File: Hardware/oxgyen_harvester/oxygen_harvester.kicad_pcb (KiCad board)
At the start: 2 copper layers, 154.9 x 111.8 mm, 79 parts, among them J1 Barrel_Jack_Switch, J10 Screw_Terminal_01x02, J11 Screw_Terminal_01x02, J12 Screw_Terminal_01x02, J13 Screw_Terminal_01x02, J14 Screw_Terminal_01x02, J15 Screw_Terminal_01x02, J16 Screw_Terminal_01x02, J17 Screw_Terminal_01x02, J18 Screw_Terminal_01x02, J19 Screw_Terminal_01x02, J2 Conn_01x20, J20 Screw_Terminal_01x02, J21 Screw_Terminal_01x02, J22 Screw_Terminal_01x02, J23 Screw_Terminal_01x02, J3 Conn_01x20, J4 Conn_01x20, J5 OLED, J6 Gas_Pressure_Sensor, J7 Gas_Flowrate_Concentration_Se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, J8 Screw_Terminal_01x02, J9 Screw_Terminal_01x02, K1 SANYOU_SRD_Form_C, K2 SANYOU_SRD_Form_C, K3 SANYOU_SRD_Form_C, K4 SANYOU_SRD_Form_C, K5 SANYOU_SRD_Form_C, K6 SANYOU_SRD_Form_C, K7 SANYOU_SRD_Form_C, K8 SANYOU_SRD_Form_C, Q1 2N2219, Q2 2N2219, Q3 2N2219, Q4 2N2219, Q5 2N2219, Q6 2N2219, Q7 2N2219, Q8 2N2219, SW1 SW_SPDT, U1 Buck_Converter, U2 Buck_Converter

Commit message: Hardware and software changes
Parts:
- J5: footprint TerminalBlock:TerminalBlock_bornier-5_P5.08mm -> TerminalBlock:TerminalBlock_bornier-4_P5.08mm
- moved SW1 5.08 mm to (218.4, 127.0), turned to 180 degrees
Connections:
- J1 pad 1: Net-(J1-Pad1) -> Net-(SW1-A)
- J3 pad 5: OLED_RST -> /general_layout/PB2
- J4 pad 5: OLED_RST -> /general_layout/PB2
- J5 pad 3: OLED_RST -> OLED_SCL
- J5 pad 4: OLED_SCL -> OLED_SDA
- SW1 pad 1: GND -> Net-(SW1-A)
- SW1 pad 2: Net-(J1-Pad1) -> +24V
- SW1 pad 3: +24V -> GND
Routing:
- net OLED_RST: track 72.4 -> 0.00 mm
- net GND: track 835.2 -> 884.5 mm
- net Net-(J1-Pad1): track 20.1 -> 0.00 mm
- net Net-(SW1-A): track 0.00 -> 11.4 mm
- net OLED_SDA: track 41.8 -> 46.9 mm
- net +24V: track 200.0 -> 204.8 mm
- net /general_layout/PB2: track 0.00 -> 3.28 mm
- net OLED_SCL: track 78.8 -> 80.9 mm

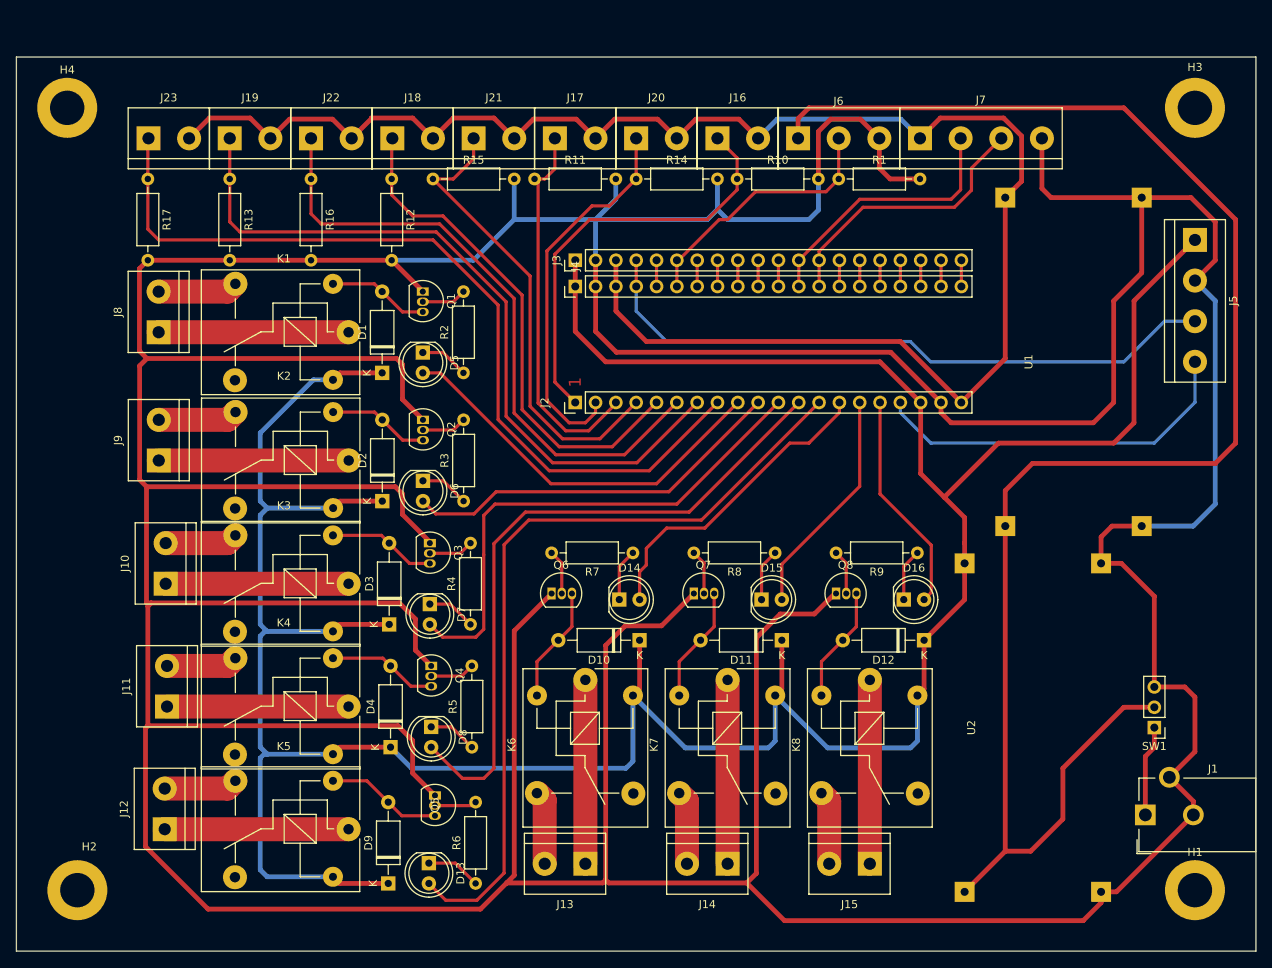
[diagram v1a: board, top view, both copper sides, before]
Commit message: Removed chamber 3 control
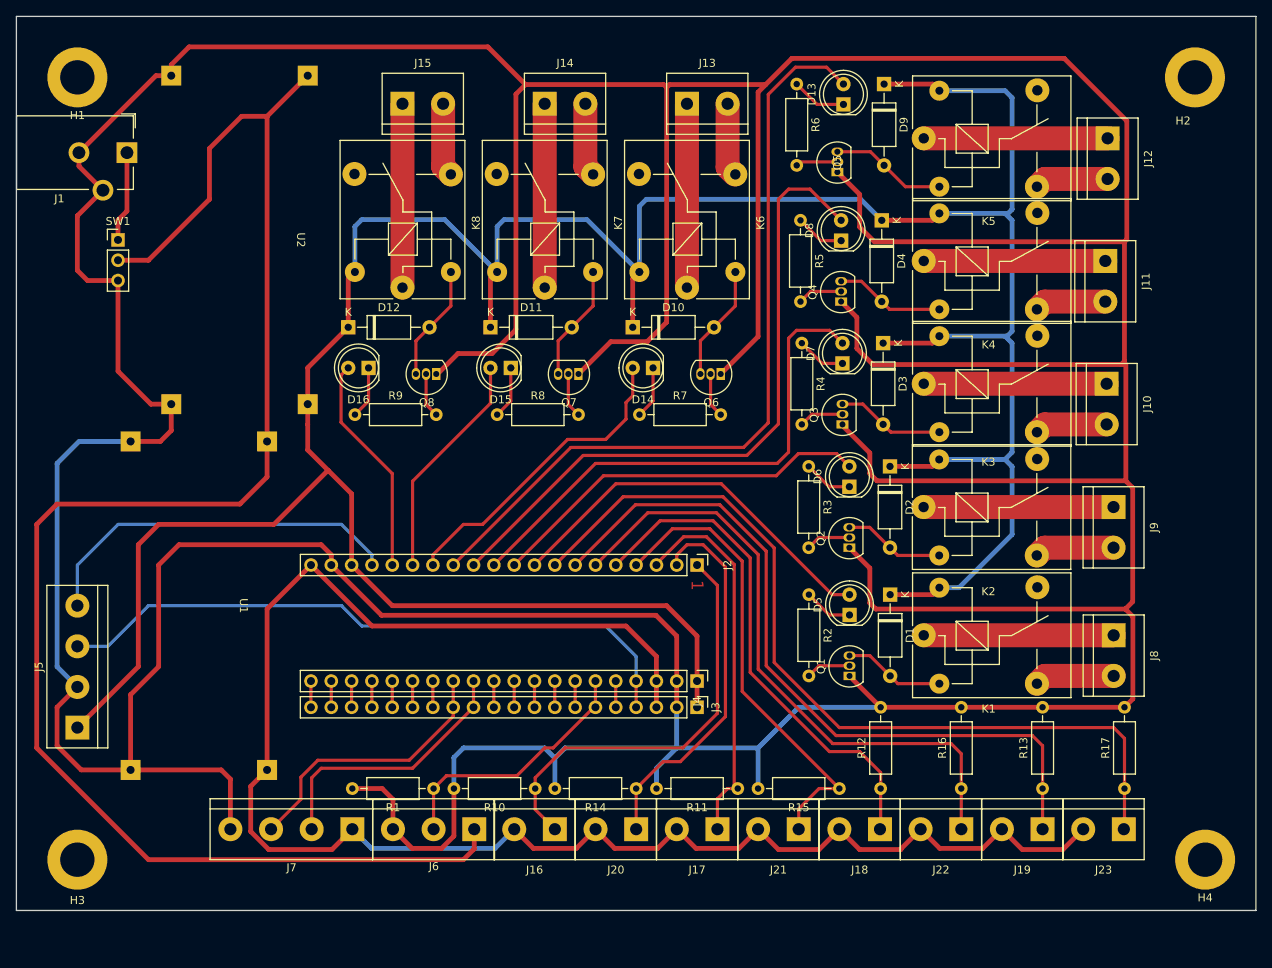
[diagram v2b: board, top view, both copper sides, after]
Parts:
- moved H1 172.7 mm to (83.8, 45.7), turned to 180 degrees
- moved H2 172.7 mm to (223.5, 45.7), turned to 180 degrees
- moved H4 170.5 mm to (224.8, 143.5), turned to 180 degrees
- moved H3 168.4 mm to (83.8, 143.5), turned to 180 degrees
- moved J5 152.4 mm to (83.8, 127.0), turned to 90 degrees
- moved J1 151.8 mm to (90.0, 55.1), turned to -90 degrees
- moved J23 149.4 mm to (214.6, 139.7), turned to 180 degrees
- moved J12 146.1 mm to (212.6, 53.3), turned to -90 degrees
- moved R17 143.9 mm to (214.7, 134.6), turned to 90 degrees
- moved SW1 143.2 mm to (88.9, 66.0), turned to 0 degrees
- moved J19 133.3 mm to (204.5, 139.7), turned to 180 degrees
- moved J11 129.8 mm to (212.3, 68.7), turned to -90 degrees
- moved R13 127.0 mm to (204.5, 134.6), turned to 90 degrees
- moved J8 125.2 mm to (213.4, 115.5), turned to -90 degrees
- moved J10 120.2 mm to (212.5, 84.0), turned to -90 degrees
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
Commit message: Latest changes in firmware hardware and documentation
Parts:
- J2, J3, J4: footprint Connector_PinHeader_2.54mm:PinHeader_1x20_P2.54mm_Vertical -> Connector_PinSocket_2.54mm:PinSocket_1x20_P2.54mm_Vertical
- SW1: footprint Connector_PinHeader_2.54mm:PinHeader_1x03_P2.54mm_Vertical -> Connector_PinSocket_2.54mm:PinSocket_1x03_P2.54mm_Vertical
